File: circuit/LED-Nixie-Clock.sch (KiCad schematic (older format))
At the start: 37 parts, among them J1 USB Micro, J2 Debug, J3 Serial, SW1 Boot0, U1 MCP1700-3302E_SOT23, U2 STM32F103C8Tx, Y1 8MHz, Y2 32.768kHz

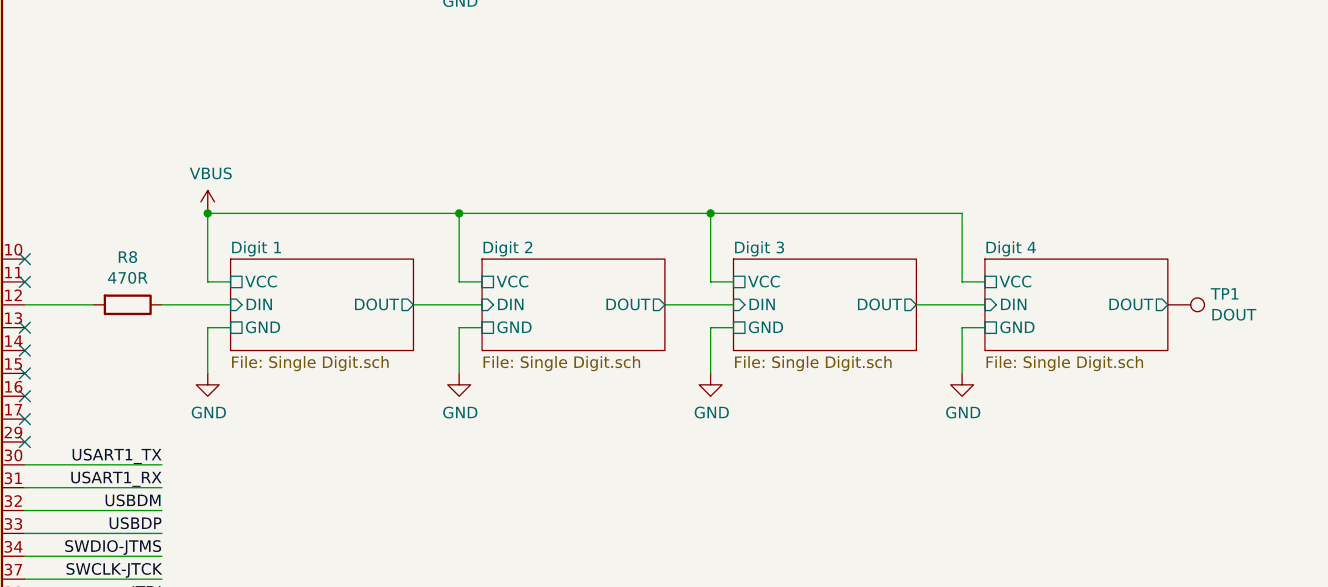
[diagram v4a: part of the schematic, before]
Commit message: Add test points for DIN and DOUT, improve front side routing
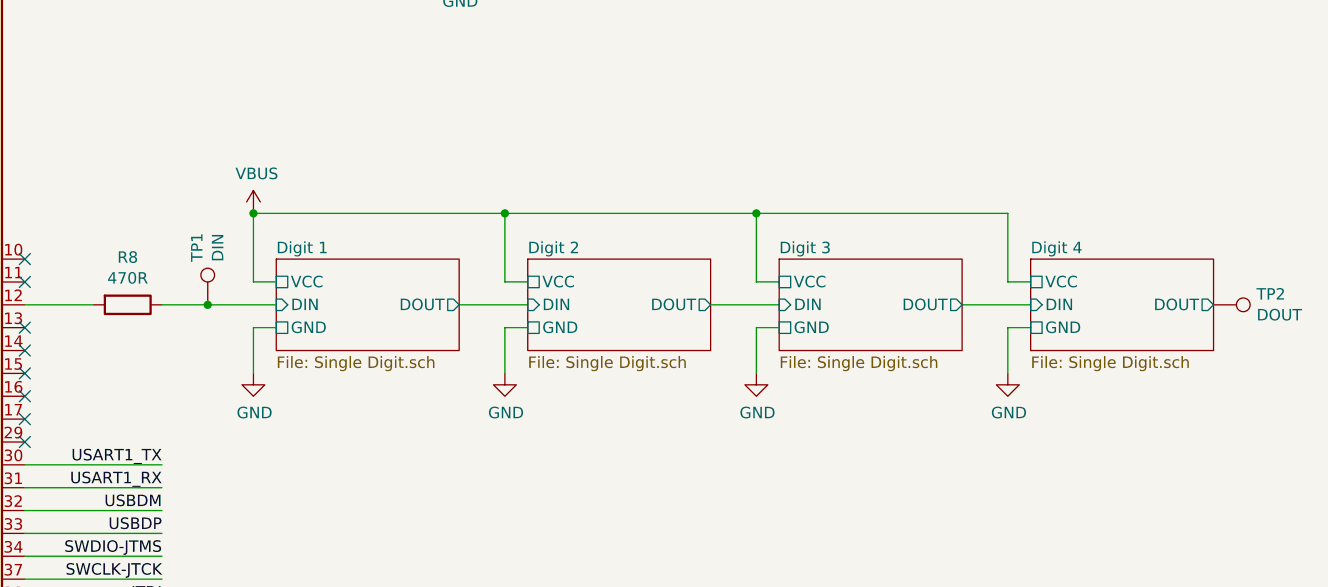
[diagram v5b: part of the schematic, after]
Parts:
- added TP1: DIN, TestPoint:TestPoint_Pad_2.5x2.5mm, symbol Connector:TestPoint
- TP2: renamed from TP1; footprint TestPoint:TestPoint_Pad_1.0x1.0mm -> TestPoint:TestPoint_Pad_2.5x2.5mm
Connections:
- net Digit 1/DIN: now also TP1.1
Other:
- moved on the sheet: TP2
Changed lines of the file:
@@
 $EndComp
 $Sheet
-S 6400 3500 800  400
+S 6600 3500 800  400
 U 5C39F816
 F0 "Digit 1" 50
 F1 "Single Digit.sch" 50
-F2 "VCC" U L 6400 3600 50
-F3 "GND" U L 6400 3800 50
-F4 "DIN" I L 6400 3700 50
-F5 "DOUT" O R 7200 3700 50
+F2 "VCC" U L 6600 3600 50
+F3 "GND" U L 6600 3800 50
+F4 "DIN" I L 6600 3700 50
+F5 "DOUT" O R 7400 3700 50
 $EndSheet
 $Comp
@@
 $EndComp
 Wire Wire Line
-	6100 3700 6400 3700
+	6300 3700 6600 3700
 $Comp
 L power:GND #PWR0113
 U 1 1 5C3A1838
-P 6300 4000
-F 0 "#PWR0113" H 6300 3750 50  0001 C CNN
-F 1 "GND" H 6305 3827 50  0000 C CNN
-F 2 "" H 6300 4000 50  0001 C CNN
-F 3 "" H 6300 4000 50  0001 C CNN
-	1    6300 4000
-	1    0    0    -1
-$EndComp
-Wire Wire Line
-	6300 3300 6300 3600
-Wire Wire Line
-	6300 3600 6400 3600
-Wire Wire Line
-	6400 3800 6300 3800
-Wire Wire Line
-	6300 3800 6300 4000
+P 6500 4000
+F 0 "#PWR0113" H 6500 3750 50  0001 C CNN
+F 1 "GND" H 6505 3827 50  0000 C CNN
+F 2 "" H 6500 4000 50  0001 C CNN
+F 3 "" H 6500 4000 50  0001 C CNN
+	1    6500 4000
+	1    0    0    -1
+$EndComp
+Wire Wire Line
+	6500 3300 6500 3600
+Wire Wire Line
+	6500 3600 6600 3600
+Wire Wire Line
+	6600 3800 6500 3800
+Wire Wire Line
+	6500 3800 6500 4000
 $Comp
 L power:VDD #PWR0157
@@
 	3600 2400 4200 2400
 $Sheet
-S 7500 3500 800  400
+S 7700 3500 800  400
 U 5C3FE993
 F0 "Digit 2" 50
 F1 "Single Digit.sch" 50
-F2 "VCC" U L 7500 3600 50
-F3 "GND" U L 7500 3800 50
-F4 "DIN" I L 7500 3700 50
-F5 "DOUT" O R 8300 3700 50
+F2 "VCC" U L 7700 3600 50
+F3 "GND" U L 7700 3800 50
+F4 "DIN" I L 7700 3700 50
+F5 "DOUT" O R 8500 3700 50
 $EndSheet
 $Comp
 L power:GND #PWR0168
 U 1 1 5C3FF583
-P 7400 4000
-F 0 "#PWR0168" H 7400 3750 50  0001 C CNN
-F 1 "GND" H 7405 3827 50  0000 C CNN
-F 2 "" H 7400 4000 50  0001 C CNN
-F 3 "" H 7400 4000 50  0001 C CNN
-	1    7400 4000
-	1    0    0    -1
-$EndComp
-Wire Wire Line
-	7400 3300 7400 3600
-Wire Wire Line
-	7400 3600 7500 3600
-Wire Wire Line
-	7500 3800 7400 3800
-Wire Wire Line
-	7400 3800 7400 4000
-Wire Wire Line
-	7200 3700 7500 3700
+P 7600 4000
+F 0 "#PWR0168" H 7600 3750 50  0001 C CNN
+F 1 "GND" H 7605 3827 50  0000 C CNN
+F 2 "" H 7600 4000 50  0001 C CNN
+F 3 "" H 7600 4000 50  0001 C CNN
+	1    7600 4000
+	1    0    0    -1
+$EndComp
+Wire Wire Line
+	7600 3300 7600 3600
+Wire Wire Line
+	7600 3600 7700 3600
+Wire Wire Line
+	7700 3800 7600 3800
+Wire Wire Line
+	7600 3800 7600 4000
+Wire Wire Line
+	7400 3700 7700 3700
 $Sheet
-S 8600 3500 800  400
+S 8800 3500 800  400
 U 5C402CAE
 F0 "Digit 3" 50
 F1 "Single Digit.sch" 50
-F2 "VCC" U L 8600 3600 50
-F3 "GND" U L 8600 3800 50
-F4 "DIN" I L 8600 3700 50
-F5 "DOUT" O R 9400 3700 50
+F2 "VCC" U L 8800 3600 50
+F3 "GND" U L 8800 3800 50
+F4 "DIN" I L 8800 3700 50
+F5 "DOUT" O R 9600 3700 50
 $EndSheet
 $Comp
 L power:GND #PWR02
 U 1 1 5C402CBB
-P 8500 4000
-F 0 "#PWR02" H 8500 3750 50  0001 C CNN
-F 1 "GND" H 8505 3827 50  0000 C CNN
-F 2 "" H 8500 4000 50  0001 C CNN
-F 3 "" H 8500 4000 50  0001 C CNN
-	1    8500 4000
-	1    0    0    -1
-$EndComp
-Wire Wire Line
-	8500 3300 8500 3600
-Wire Wire Line
-	8500 3600 8600 3600
-Wire Wire Line
-	8600 3800 8500 3800
-Wire Wire Line
-	8500 3800 8500 4000
+P 8700 4000
+F 0 "#PWR02" H 8700 3750 50  0001 C CNN
+F 1 "GND" H 8705 3827 50  0000 C CNN
+F 2 "" H 8700 4000 50  0001 C CNN
+F 3 "" H 8700 4000 50  0001 C CNN
+	1    8700 4000
+	1    0    0    -1
+$EndComp
+Wire Wire Line
+	8700 3300 8700 3600
+Wire Wire Line
+	8700 3600 8800 3600
+Wire Wire Line
+	8800 3800 8700 3800
+Wire Wire Line
+	8700 3800 8700 4000
 $Sheet
-S 9700 3500 800  400
+S 9900 3500 800  400
 U 5C402CC5
 F0 "Digit 4" 50
 F1 "Single Digit.sch" 50
-F2 "VCC" U L 9700 3600 50
-F3 "GND" U L 9700 3800 50
-F4 "DIN" I L 9700 3700 50
-F5 "DOUT" O R 10500 3700 50
+F2 "VCC" U L 9900 3600 50
+F3 "GND" U L 9900 3800 50
+F4 "DIN" I L 9900 3700 50
+F5 "DOUT" O R 10700 3700 50
 $EndSheet
 $Comp
 L power:GND #PWR04
 U 1 1 5C402CD2
-P 9600 4000
-F 0 "#PWR04" H 9600 3750 50  0001 C CNN
-F 1 "GND" H 9605 3827 50  0000 C CNN
-F 2 "" H 9600 4000 50  0001 C CNN
-F 3 "" H 9600 4000 50  0001 C CNN
-	1    9600 4000
-	1    0    0    -1
-$EndComp
-Wire Wire Line
-	9600 3600 9700 3600
-Wire Wire Line
-	9700 3800 9600 3800
-Wire Wire Line
-	9600 3800 9600 4000
-Wire Wire Line
-	9400 3700 9700 3700
-Wire Wire Line
-	8300 3700 8600 3700
+P 9800 4000
+F 0 "#PWR04" H 9800 3750 50  0001 C CNN
+F 1 "GND" H 9805 3827 50  0000 C CNN
+F 2 "" H 9800 4000 50  0001 C CNN
+F 3 "" H 9800 4000 50  0001 C CNN
+	1    9800 4000
+	1    0    0    -1
+$EndComp
+Wire Wire Line
+	9800 3600 9900 3600
+Wire Wire Line
+	9900 3800 9800 3800
+Wire Wire Line
+	9800 3800 9800 4000
+Wire Wire Line
+	9600 3700 9900 3700
+Wire Wire Line
+	8500 3700 8800 3700
 $Comp
 L Switch:SW_Push SW1
@@
 $EndComp
 Wire Wire Line
-	6300 3300 7400 3300
-Wire Wire Line
-	9600 3300 9600 3600
-Connection ~ 8500 3300
-Wire Wire Line
-	8500 3300 9600 3300
-Connection ~ 7400 3300
-Wire Wire Line
-	7400 3300 8500 3300
+	6500 3300 7600 3300
+Wire Wire Line
+	9800 3300 9800 3600
+Connection ~ 8700 3300
+Wire Wire Line
+	8700 3300 9800 3300
+Connection ~ 7600 3300
+Wire Wire Line
+	7600 3300 8700 3300
 Connection ~ 4800 2200
 Wire Wire Line
@@
 L power:VBUS #PWR0112
 U 1 1 5C5B244A
-P 6300 3300
-F 0 "#PWR0112" H 6300 3150 50  0001 C CNN
-F 1 "VBUS" H 6315 3473 50  0000 C CNN
-F 2 "" H 6300 3300 50  0001 C CNN
-F 3 "" H 6300 3300 50  0001 C CNN
-	1    6300 3300
-	1    0    0    -1
-$EndComp
-Connection ~ 6300 3300
+P 6500 3300
+F 0 "#PWR0112" H 6500 3150 50  0001 C CNN
+F 1 "VBUS" H 6515 3473 50  0000 C CNN
+F 2 "" H 6500 3300 50  0001 C CNN
+F 3 "" H 6500 3300 50  0001 C CNN
+	1    6500 3300
+	1    0    0    -1
+$EndComp
+Connection ~ 6500 3300
 Wire Wire Line
 	2700 800  2700 1050
@@
 $EndComp
 $Comp
-L Connector:TestPoint TP1
+L Connector:TestPoint TP2
 U 1 1 5C8AE386
-P 10500 3700
-F 0 "TP1" V 10454 3888 50  0000 L CNN
-F 1 "DOUT" V 10545 3888 50  0000 L CNN
-F 2 "TestPoint:TestPoint_Pad_1.0x1.0mm" H 10700 3700 50  0001 C CNN
-F 3 "~" H 10700 3700 50  0001 C CNN
-	1    10500 3700
+P 10700 3700
+F 0 "TP2" V 10654 3888 50  0000 L CNN
+F 1 "DOUT" V 10745 3888 50  0000 L CNN
+F 2 "TestPoint:TestPoint_Pad_2.5x2.5mm" H 10900 3700 50  0001 C CNN
+F 3 "~" H 10900 3700 50  0001 C CNN
+	1    10700 3700
 	0    1    1    0
 $EndComp
@@
 Connection ~ 1000 1600
 Connection ~ 1300 1600
+$Comp
+L Connector:TestPoint TP1
+U 1 1 5DB5B6B1
+P 6300 3700
+F 0 "TP1" V 6254 3888 50  0000 L CNN
+F 1 "DIN" V 6345 3888 50  0000 L CNN
+F 2 "TestPoint:TestPoint_Pad_2.5x2.5mm" H 6500 3700 50  0001 C CNN
+F 3 "~" H 6500 3700 50  0001 C CNN
+	1    6300 3700
+	1    0    0    -1
+$EndComp
+Wire Wire Line
+	6300 3700 6100 3700
+Connection ~ 6300 3700
 $EndSCHEMATC

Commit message: Add input buttons
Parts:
- added H7: MountingHole, MountingHole:MountingHole_3.2mm_M3_ISO7380, symbol Mechanical:MountingHole
- added R10, R11, R12, R9: 100k, Resistor_SMD:R_0805_2012Metric_Pad1.15x1.40mm_HandSolder, symbol Device:R
- added SW2: Button \"Back\", Button_Switch_SMD:SW_Push_1P1T_NO_6x6mm_H9.5mm, symbol Switch:SW_Push
- added SW3: Button \"-\", Button_Switch_SMD:SW_Push_1P1T_NO_6x6mm_H9.5mm, symbol Switch:SW_Push
- added SW4: Button \"+\", Button_Switch_SMD:SW_Push_1P1T_NO_6x6mm_H9.5mm, symbol Switch:SW_Push
- added SW5: Button \"Ok\", Button_Switch_SMD:SW_Push_1P1T_NO_6x6mm_H9.5mm, symbol Switch:SW_Push
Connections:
- net GND: now also SW2.1, SW3.1, SW4.1, SW5.1
- net VDD: now also R10.2, R11.2, R12.2, R9.2
- net BTN3: now reaches U2.14 (PA4)
- net BTN3: now also R12.1, SW5.2
- net BTN2: now reaches U2.15 (PA5)
- net BTN2: now also R11.1, SW4.2
- net BTN1: now reaches U2.16 (PA6)
- net BTN1: now also R10.1, SW3.2
- net BTN0: now reaches U2.17 (PA7)
- net BTN0: now also R9.1, SW2.2
- no-connect marks 23 -> 19
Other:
- moved on the sheet: H1, H2, H3, H4, H5, H6

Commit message: Enlarge PCB and add more mounting holes
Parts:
- added H1, H5, H6, H9: MountingHole, MountingHole:MountingHole_3.2mm_M3_ISO7380, symbol Mechanical:MountingHole
- renumbered H6 to H10, H7 to H11, H1 to H2, H2 to H3, H3 to H4, H4 to H7, H5 to H8
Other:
- moved on the sheet: H2, H3, H4, H7, H8
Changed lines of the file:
@@
 Connection ~ 3300 1600
 $Comp
-L Mechanical:MountingHole H6
+L Mechanical:MountingHole H10
 U 1 1 5C8F568C
 P 600 7500
-F 0 "H6" H 700 7546 50  0000 L CNN
+F 0 "H10" H 700 7546 50  0000 L CNN
 F 1 "MountingHole" H 700 7455 50  0000 L CNN
 F 2 "MountingHole:MountingHole_3.2mm_M3_ISO7380" H 600 7500 50  0001 C CNN
@@
 $EndComp
 $Comp
-L Mechanical:MountingHole H5
+L Mechanical:MountingHole H8
 U 1 1 5C8F5A1B
-P 600 7300
-F 0 "H5" H 700 7346 50  0000 L CNN
-F 1 "MountingHole" H 700 7255 50  0000 L CNN
-F 2 "MountingHole:MountingHole_3.2mm_M3_ISO7380" H 600 7300 50  0001 C CNN
-F 3 "~" H 600 7300 50  0001 C CNN
-	1    600  7300
-	1    0    0    -1
-$EndComp
-$Comp
-L Mechanical:MountingHole H4
-U 1 1 5C8F5ADF
 P 600 7100
-F 0 "H4" H 700 7146 50  0000 L CNN
+F 0 "H8" H 700 7146 50  0000 L CNN
 F 1 "MountingHole" H 700 7055 50  0000 L CNN
 F 2 "MountingHole:MountingHole_3.2mm_M3_ISO7380" H 600 7100 50  0001 C CNN
@@
 $EndComp
 $Comp
-L Mechanical:MountingHole H3
-U 1 1 5C8F5CA1
+L Mechanical:MountingHole H7
+U 1 1 5C8F5ADF
 P 600 6900
-F 0 "H3" H 700 6946 50  0000 L CNN
+F 0 "H7" H 700 6946 50  0000 L CNN
 F 1 "MountingHole" H 700 6855 50  0000 L CNN
 F 2 "MountingHole:MountingHole_3.2mm_M3_ISO7380" H 600 6900 50  0001 C CNN
@@
 $EndComp
 $Comp
+L Mechanical:MountingHole H4
+U 1 1 5C8F5CA1
+P 600 6300
+F 0 "H4" H 700 6346 50  0000 L CNN
+F 1 "MountingHole" H 700 6255 50  0000 L CNN
+F 2 "MountingHole:MountingHole_3.2mm_M3_ISO7380" H 600 6300 50  0001 C CNN
+F 3 "~" H 600 6300 50  0001 C CNN
+	1    600  6300
+	1    0    0    -1
+$EndComp
+$Comp
+L Mechanical:MountingHole H3
+U 1 1 5C8F5DF1
+P 600 6100
+F 0 "H3" H 700 6146 50  0000 L CNN
+F 1 "MountingHole" H 700 6055 50  0000 L CNN
+F 2 "MountingHole:MountingHole_3.2mm_M3_ISO7380" H 600 6100 50  0001 C CNN
+F 3 "~" H 600 6100 50  0001 C CNN
+	1    600  6100
+	1    0    0    -1
+$EndComp
+$Comp
 L Mechanical:MountingHole H2
-U 1 1 5C8F5DF1
-P 600 6700
-F 0 "H2" H 700 6746 50  0000 L CNN
-F 1 "MountingHole" H 700 6655 50  0000 L CNN
-F 2 "MountingHole:MountingHole_3.2mm_M3_ISO7380" H 600 6700 50  0001 C CNN
-F 3 "~" H 600 6700 50  0001 C CNN
-	1    600  6700
-	1    0    0    -1
-$EndComp
-$Comp
-L Mechanical:MountingHole H1
 U 1 1 5C8F5EE9
-P 600 6500
-F 0 "H1" H 700 6546 50  0000 L CNN
-F 1 "MountingHole" H 700 6455 50  0000 L CNN
-F 2 "MountingHole:MountingHole_3.2mm_M3_ISO7380" H 600 6500 50  0001 C CNN
-F 3 "~" H 600 6500 50  0001 C CNN
-	1    600  6500
+P 600 5900
+F 0 "H2" H 700 5946 50  0000 L CNN
+F 1 "MountingHole" H 700 5855 50  0000 L CNN
+F 2 "MountingHole:MountingHole_3.2mm_M3_ISO7380" H 600 5900 50  0001 C CNN
+F 3 "~" H 600 5900 50  0001 C CNN
+	1    600  5900
 	1    0    0    -1
 $EndComp
@@
 BTN0
 $Comp
-L Mechanical:MountingHole H7
+L Mechanical:MountingHole H11
 U 1 1 5DBF1BFA
 P 600 7700
-F 0 "H7" H 700 7746 50  0000 L CNN
+F 0 "H11" H 700 7746 50  0000 L CNN
 F 1 "MountingHole" H 700 7655 50  0000 L CNN
 F 2 "MountingHole:MountingHole_3.2mm_M3_ISO7380" H 600 7700 50  0001 C CNN
@@
 	1    0    0    -1
 $EndComp
+$Comp
+L Mechanical:MountingHole H1
+U 1 1 5DC3D8E0
+P 600 5700
+F 0 "H1" H 700 5746 50  0000 L CNN
+F 1 "MountingHole" H 700 5655 50  0000 L CNN
+F 2 "MountingHole:MountingHole_3.2mm_M3_ISO7380" H 600 5700 50  0001 C CNN
+F 3 "~" H 600 5700 50  0001 C CNN
+	1    600  5700
+	1    0    0    -1
+$EndComp
+$Comp
+L Mechanical:MountingHole H5
+U 1 1 5DC3DBF4
+P 600 6500
+F 0 "H5" H 700 6546 50  0000 L CNN
+F 1 "MountingHole" H 700 6455 50  0000 L CNN
+F 2 "MountingHole:MountingHole_3.2mm_M3_ISO7380" H 600 6500 50  0001 C CNN
+F 3 "~" H 600 6500 50  0001 C CNN
+	1    600  6500
+	1    0    0    -1
+$EndComp
+$Comp
+L Mechanical:MountingHole H6
+U 1 1 5DC3DFF6
+P 600 6700
+F 0 "H6" H 700 6746 50  0000 L CNN
+F 1 "MountingHole" H 700 6655 50  0000 L CNN
+F 2 "MountingHole:MountingHole_3.2mm_M3_ISO7380" H 600 6700 50  0001 C CNN
+F 3 "~" H 600 6700 50  0001 C CNN
+	1    600  6700
+	1    0    0    -1
+$EndComp
+$Comp
+L Mechanical:MountingHole H9
+U 1 1 5DC3E54C
+P 600 7300
+F 0 "H9" H 700 7346 50  0000 L CNN
+F 1 "MountingHole" H 700 7255 50  0000 L CNN
+F 2 "MountingHole:MountingHole_3.2mm_M3_ISO7380" H 600 7300 50  0001 C CNN
+F 3 "~" H 600 7300 50  0001 C CNN
+	1    600  7300
+	1    0    0    -1
+$EndComp
